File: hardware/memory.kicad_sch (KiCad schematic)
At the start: 5 parts, among them U2 ICE40HX4K-TQ144

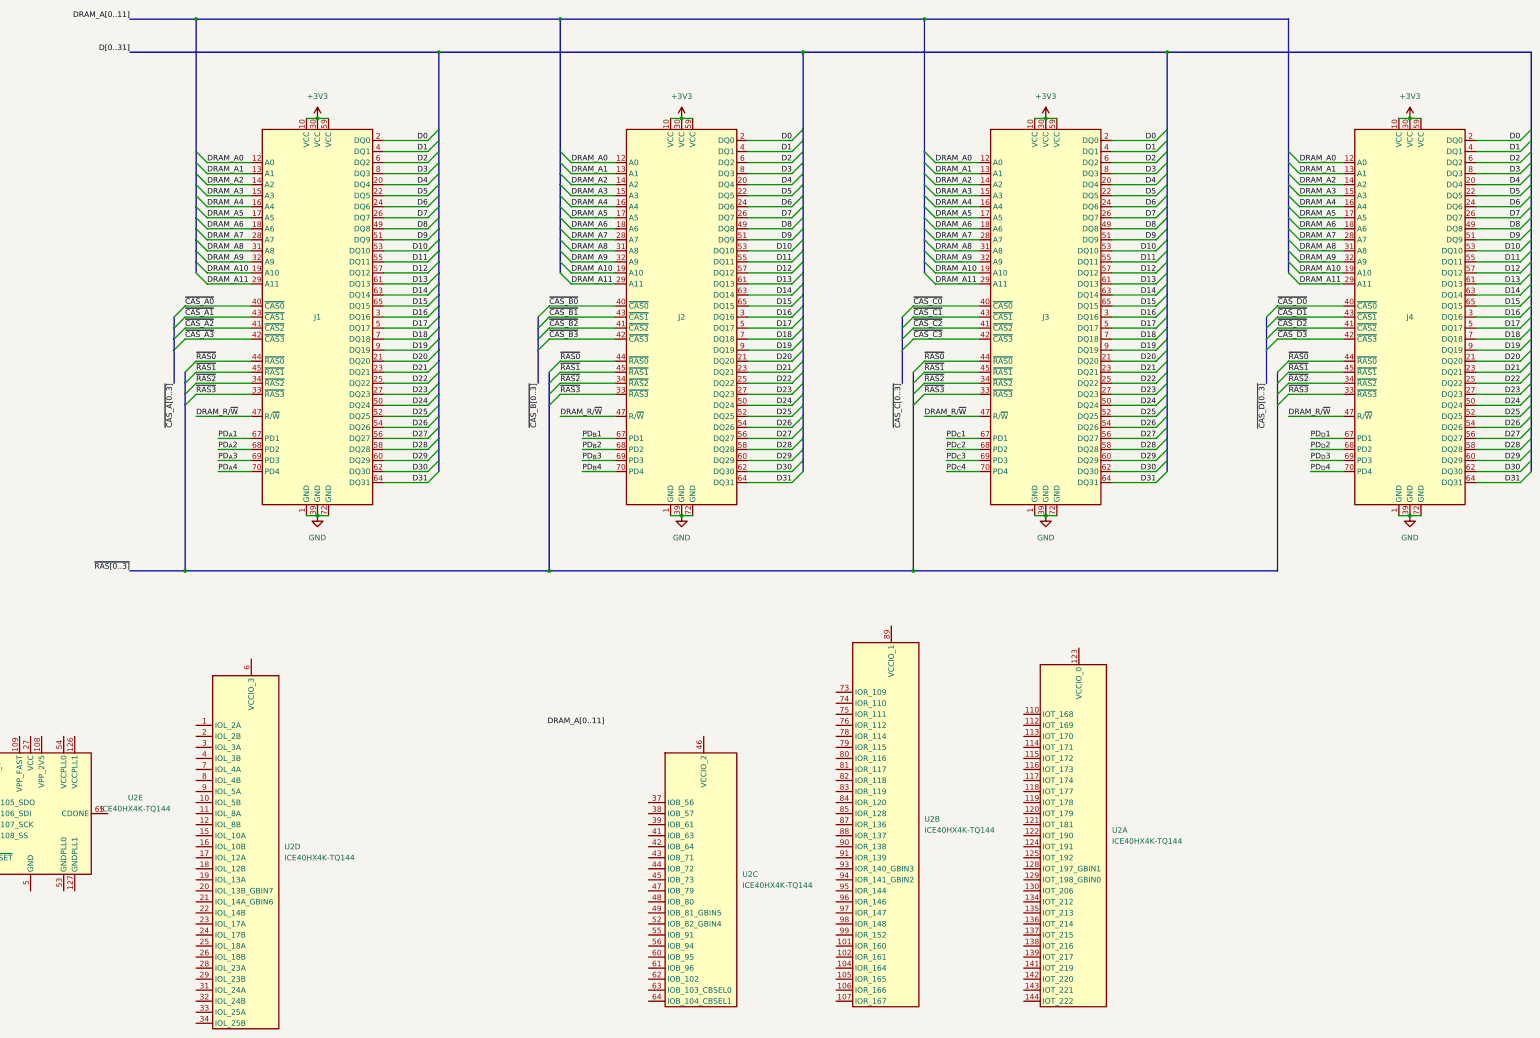
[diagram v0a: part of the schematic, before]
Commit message: more memory wiring
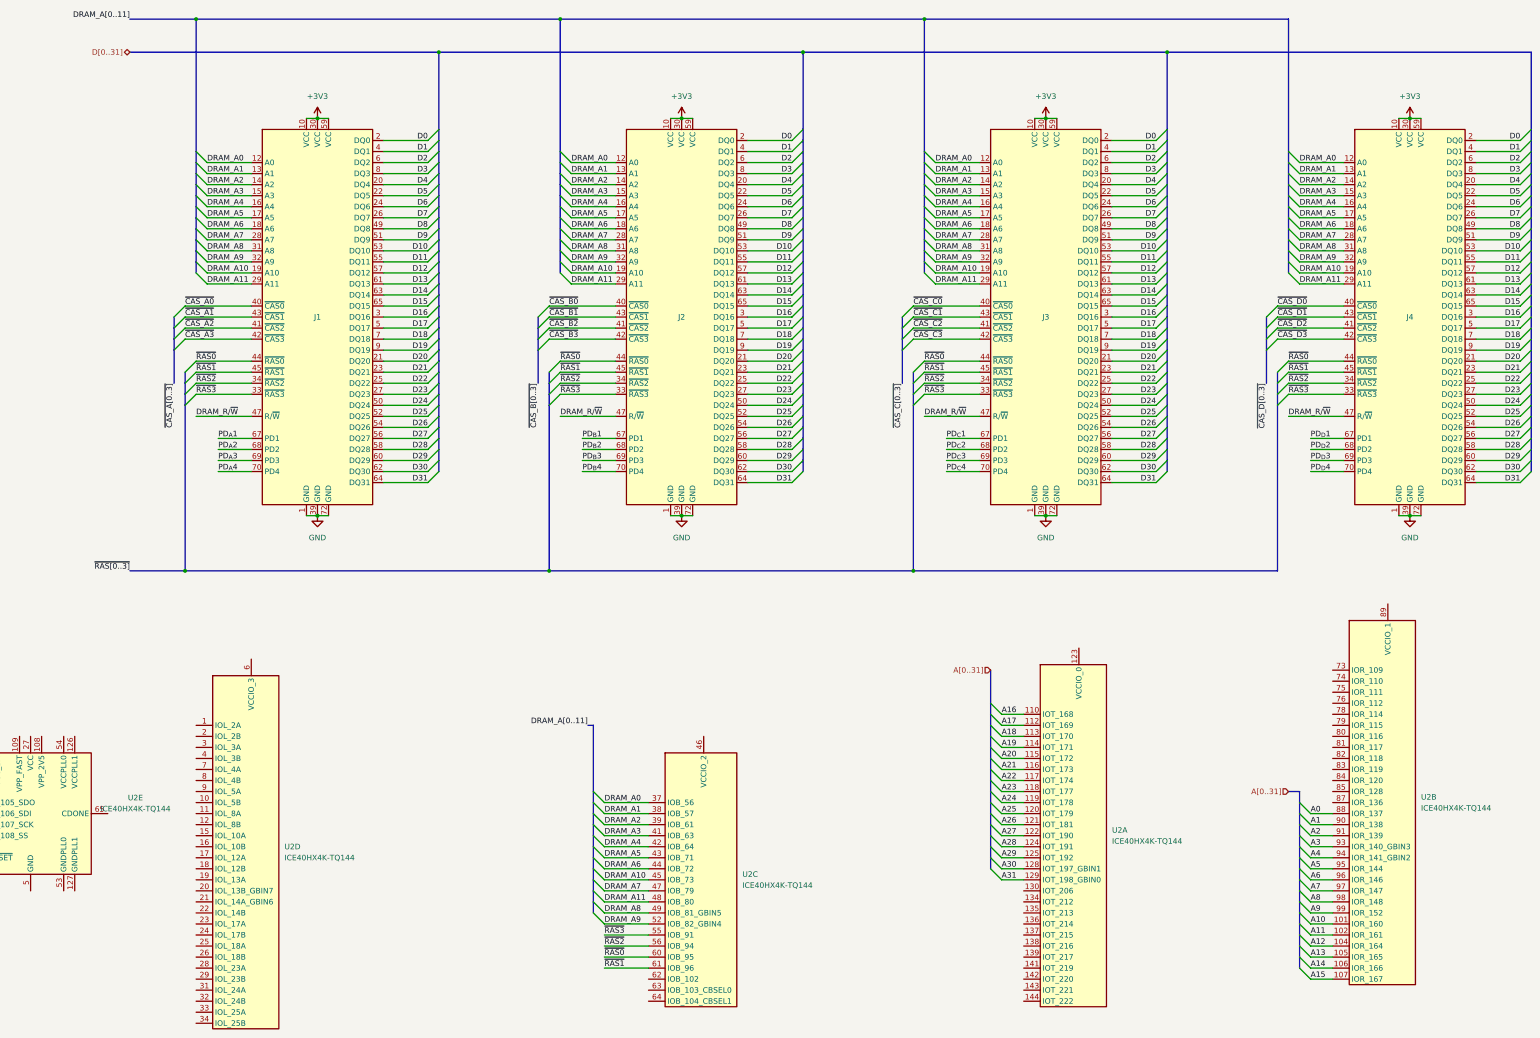
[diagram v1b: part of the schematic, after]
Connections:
- net DRAM_A0: now also U2.37 (IOB_56)
- net DRAM_A1: now also U2.38 (IOB_57)
- net DRAM_A10: now also U2.45 (IOB_73)
- net DRAM_A11: now also U2.48 (IOB_80)
- net DRAM_A2: now also U2.39 (IOB_61)
- net DRAM_A3: now also U2.41 (IOB_63)
- net DRAM_A4: now also U2.42 (IOB_64)
- net DRAM_A5: now also U2.43 (IOB_71)
- net DRAM_A6: now also U2.44 (IOB_72)
- net DRAM_A7: now also U2.47 (IOB_79)
- net DRAM_A8: now also U2.49 (IOB_81_GBIN5)
- net DRAM_A9: now also U2.52 (IOB_82_GBIN4)
- net ~{RAS0}: now also U2.60 (IOB_95)
- net ~{RAS1}: now also U2.61 (IOB_96)
- net ~{RAS2}: now also U2.56 (IOB_94)
- net ~{RAS3}: now also U2.55 (IOB_91)
- net A10: now reaches U2.101 (IOR_160)
- net A11: now reaches U2.102 (IOR_161)
- net A12: now reaches U2.104 (IOR_164)
- net A13: now reaches U2.105 (IOR_165)
- net A14: now reaches U2.106 (IOR_166)
- net A15: now reaches U2.107 (IOR_167)
- net A0: now reaches U2.88 (IOR_137)
- net A1: now reaches U2.90 (IOR_138)
- net A2: now reaches U2.91 (IOR_139)
- net A3: now reaches U2.93 (IOR_140_GBIN3)
- net A4: now reaches U2.94 (IOR_141_GBIN2)
- net A5: now reaches U2.95 (IOR_144)
- net A6: now reaches U2.96 (IOR_146)
- net A7: now reaches U2.97 (IOR_147)
- net A8: now reaches U2.98 (IOR_148)
- net A9: now reaches U2.99 (IOR_152)
- net A16: now reaches U2.110 (IOT_168)
- net A17: now reaches U2.112 (IOT_169)
- net A18: now reaches U2.113 (IOT_170)
- net A19: now reaches U2.114 (IOT_171)
- net A20: now reaches U2.115 (IOT_172)
- net A21: now reaches U2.116 (IOT_173)
- net A22: now reaches U2.117 (IOT_174)
- net A23: now reaches U2.118 (IOT_177)
- net A24: now reaches U2.119 (IOT_178)
- net A25: now reaches U2.120 (IOT_179)
- net A26: now reaches U2.121 (IOT_181)
- net A27: now reaches U2.122 (IOT_190)
- net A28: now reaches U2.124 (IOT_191)
- net A29: now reaches U2.125 (IOT_192)
- net A30: now reaches U2.128 (IOT_197_GBIN1)
- net A31: now reaches U2.129 (IOT_198_GBIN0)
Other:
- moved on the sheet: U2B

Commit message: lock position of expansion slots
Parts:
- J1, J2, J3, J4: footprint 68040:SIMM-72_23DEG -> 68040:SIMM-72
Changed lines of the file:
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@@
       (effects (font (size 1.27 1.27)))
     )
-    (property "Footprint" "68040:SIMM-72_23DEG" (at 287.02 99.06 0)
+    (property "Footprint" "68040:SIMM-72" (at 287.02 99.06 0)
       (effects (font (size 1.27 1.27)) hide)
     )
@@
       (effects (font (size 1.27 1.27)))
     )
-    (property "Footprint" "68040:SIMM-72_23DEG" (at 203.2 99.06 0)
+    (property "Footprint" "68040:SIMM-72" (at 203.2 99.06 0)
       (effects (font (size 1.27 1.27)) hide)
     )
@@
       (effects (font (size 1.27 1.27)))
     )
-    (property "Footprint" "68040:SIMM-72_23DEG" (at 119.38 99.06 0)
+    (property "Footprint" "68040:SIMM-72" (at 119.38 99.06 0)
       (effects (font (size 1.27 1.27)) hide)
     )
@@
       (effects (font (size 1.27 1.27)))
     )
-    (property "Footprint" "68040:SIMM-72_23DEG" (at 370.84 99.06 0)
-      (effects (font (size 1.27 1.27)) hide)
-    )
+    (property "Footprint" "68040:SIMM-72" (at 370.84 99.06 0)
+      (effects (font (size 1.27 1.27)) hide)
+    )

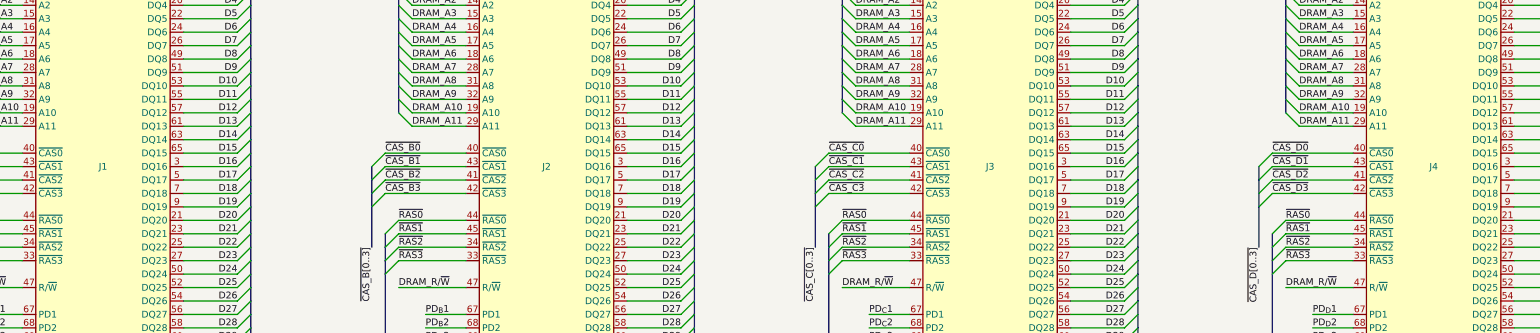
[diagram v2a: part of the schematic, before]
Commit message: fix EXP connector positioning
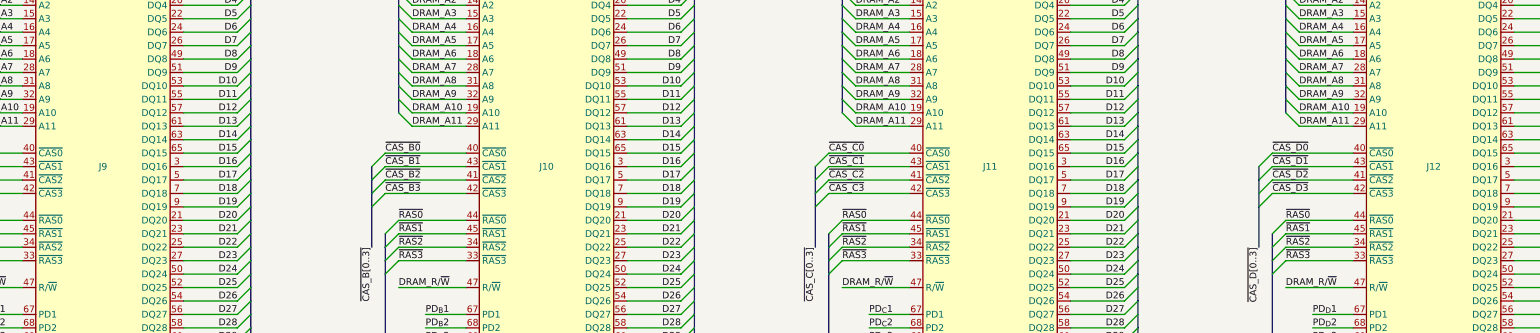
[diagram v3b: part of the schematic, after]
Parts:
- renumbered J2 to J10, J3 to J11, J4 to J12, J1 to J9
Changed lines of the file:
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@@
   (symbol (lib_id "power:+3V3") (at 203.2 55.88 0) (unit 1)
     (in_bom yes) (on_board yes) (dnp no) (fields_autoplaced)
-    (property "Reference" "#PWR07" (at 203.2 59.69 0)
+    (property "Reference" "#PWR03" (at 203.2 59.69 0)
       (effects (font (size 1.27 1.27)) hide)
     )
@@
       (project "68040pc"
         (path "/3006deba-2100-40f8-9f39-987a5c2c14c7/f9007ce6-1d62-4428-abf8-f7bfb8f1e86d"
-          (reference "#PWR07") (unit 1)
+          (reference "#PWR03") (unit 1)
         )
       )
@@
   (symbol (lib_id "power:GND") (at 203.2 147.32 0) (unit 1)
     (in_bom yes) (on_board yes) (dnp no) (fields_autoplaced)
-    (property "Reference" "#PWR02" (at 203.2 153.67 0)
+    (property "Reference" "#PWR04" (at 203.2 153.67 0)
       (effects (font (size 1.27 1.27)) hide)
     )
@@
       (project "68040pc"
         (path "/3006deba-2100-40f8-9f39-987a5c2c14c7/f9007ce6-1d62-4428-abf8-f7bfb8f1e86d"
-          (reference "#PWR02") (unit 1)
+          (reference "#PWR04") (unit 1)
         )
       )
@@
   (symbol (lib_id "68040:SIMM72_Socket") (at 287.02 101.6 0) (unit 1)
     (in_bom yes) (on_board yes) (dnp no) (fields_autoplaced)
-    (property "Reference" "J3" (at 287.02 101.6 0)
+    (property "Reference" "J11" (at 287.02 101.6 0)
       (effects (font (size 1.27 1.27)))
     )
@@
       (project "68040pc"
         (path "/3006deba-2100-40f8-9f39-987a5c2c14c7/f9007ce6-1d62-4428-abf8-f7bfb8f1e86d"
-          (reference "J3") (unit 1)
+          (reference "J11") (unit 1)
         )
       )
@@
   (symbol (lib_id "power:+3V3") (at 370.84 55.88 0) (unit 1)
     (in_bom yes) (on_board yes) (dnp no) (fields_autoplaced)
-    (property "Reference" "#PWR05" (at 370.84 59.69 0)
+    (property "Reference" "#PWR07" (at 370.84 59.69 0)
       (effects (font (size 1.27 1.27)) hide)
     )
@@
       (project "68040pc"
         (path "/3006deba-2100-40f8-9f39-987a5c2c14c7/f9007ce6-1d62-4428-abf8-f7bfb8f1e86d"
-          (reference "#PWR05") (unit 1)
+          (reference "#PWR07") (unit 1)
         )
       )
@@
   (symbol (lib_id "power:GND") (at 370.84 147.32 0) (unit 1)
     (in_bom yes) (on_board yes) (dnp no) (fields_autoplaced)
-    (property "Reference" "#PWR04" (at 370.84 153.67 0)
+    (property "Reference" "#PWR08" (at 370.84 153.67 0)
       (effects (font (size 1.27 1.27)) hide)
     )
@@
       (project "68040pc"
         (path "/3006deba-2100-40f8-9f39-987a5c2c14c7/f9007ce6-1d62-4428-abf8-f7bfb8f1e86d"
-          (reference "#PWR04") (unit 1)
+          (reference "#PWR08") (unit 1)
         )
       )
@@
   (symbol (lib_id "68040:SIMM72_Socket") (at 203.2 101.6 0) (unit 1)
     (in_bom yes) (on_board yes) (dnp no) (fields_autoplaced)
-    (property "Reference" "J2" (at 203.2 101.6 0)
+    (property "Reference" "J10" (at 203.2 101.6 0)
       (effects (font (size 1.27 1.27)))
     )
@@
       (project "68040pc"
         (path "/3006deba-2100-40f8-9f39-987a5c2c14c7/f9007ce6-1d62-4428-abf8-f7bfb8f1e86d"
-          (reference "J2") (unit 1)
+          (reference "J10") (unit 1)
         )
       )
@@
   (symbol (lib_id "68040:SIMM72_Socket") (at 119.38 101.6 0) (unit 1)
     (in_bom yes) (on_board yes) (dnp no) (fields_autoplaced)
-    (property "Reference" "J1" (at 119.38 101.6 0)
+    (property "Reference" "J9" (at 119.38 101.6 0)
       (effects (font (size 1.27 1.27)))
     )
@@
       (project "68040pc"
         (path "/3006deba-2100-40f8-9f39-987a5c2c14c7/f9007ce6-1d62-4428-abf8-f7bfb8f1e86d"
-          (reference "J1") (unit 1)
+          (reference "J9") (unit 1)
         )
       )
@@
   (symbol (lib_id "power:+3V3") (at 287.02 55.88 0) (unit 1)
     (in_bom yes) (on_board yes) (dnp no) (fields_autoplaced)
-    (property "Reference" "#PWR06" (at 287.02 59.69 0)
+    (property "Reference" "#PWR05" (at 287.02 59.69 0)
       (effects (font (size 1.27 1.27)) hide)
     )
@@
       (project "68040pc"
         (path "/3006deba-2100-40f8-9f39-987a5c2c14c7/f9007ce6-1d62-4428-abf8-f7bfb8f1e86d"
-          (reference "#PWR06") (unit 1)
+          (reference "#PWR05") (unit 1)
         )
       )
@@
   (symbol (lib_id "power:GND") (at 119.38 147.32 0) (unit 1)
     (in_bom yes) (on_board yes) (dnp no) (fields_autoplaced)
-    (property "Reference" "#PWR03" (at 119.38 153.67 0)
+    (property "Reference" "#PWR02" (at 119.38 153.67 0)
       (effects (font (size 1.27 1.27)) hide)
     )
@@
       (project "68040pc"
         (path "/3006deba-2100-40f8-9f39-987a5c2c14c7/f9007ce6-1d62-4428-abf8-f7bfb8f1e86d"
-          (reference "#PWR03") (unit 1)
+          (reference "#PWR02") (unit 1)
         )
       )
@@
   (symbol (lib_id "power:GND") (at 287.02 147.32 0) (unit 1)
     (in_bom yes) (on_board yes) (dnp no) (fields_autoplaced)
-    (property "Reference" "#PWR01" (at 287.02 153.67 0)
+    (property "Reference" "#PWR06" (at 287.02 153.67 0)
       (effects (font (size 1.27 1.27)) hide)
     )
@@
       (project "68040pc"
         (path "/3006deba-2100-40f8-9f39-987a5c2c14c7/f9007ce6-1d62-4428-abf8-f7bfb8f1e86d"
+          (reference "#PWR06") (unit 1)
+        )
+      )
+    )
+  )
+  (symbol (lib_id "power:+3V3") (at 119.38 55.88 0) (unit 1)
+    (in_bom yes) (on_board yes) (dnp no) (fields_autoplaced)
+    (property "Reference" "#PWR01" (at 119.38 59.69 0)
+      (effects (font (size 1.27 1.27)) hide)
+    )
+    (property "Value" "+3V3" (at 119.38 50.8 0)
+      (effects (font (size 1.27 1.27)))
+    )
+    (property "Footprint" "" (at 119.38 55.88 0)
+      (effects (font (size 1.27 1.27)) hide)
+    )
+    (property "Datasheet" "" (at 119.38 55.88 0)
+      (effects (font (size 1.27 1.27)) hide)
+    )
+    (pin "1")
+    (instances
+      (project "68040pc"
+        (path "/3006deba-2100-40f8-9f39-987a5c2c14c7/f9007ce6-1d62-4428-abf8-f7bfb8f1e86d"
           (reference "#PWR01") (unit 1)
         )
@@
     )
   )
-  (symbol (lib_id "power:+3V3") (at 119.38 55.88 0) (unit 1)
-    (in_bom yes) (on_board yes) (dnp no) (fields_autoplaced)
-    (property "Reference" "#PWR08" (at 119.38 59.69 0)
-      (effects (font (size 1.27 1.27)) hide)
-    )
-    (property "Value" "+3V3" (at 119.38 50.8 0)
-      (effects (font (size 1.27 1.27)))
-    )
-    (property "Footprint" "" (at 119.38 55.88 0)
-      (effects (font (size 1.27 1.27)) hide)
-    )
-    (property "Datasheet" "" (at 119.38 55.88 0)
-      (effects (font (size 1.27 1.27)) hide)
-    )
-    (pin "1")
-    (instances
-      (project "68040pc"
-        (path "/3006deba-2100-40f8-9f39-987a5c2c14c7/f9007ce6-1d62-4428-abf8-f7bfb8f1e86d"
-          (reference "#PWR08") (unit 1)
-        )
-      )
-    )
-  )
   (symbol (lib_id "68040:SIMM72_Socket") (at 370.84 101.6 0) (unit 1)
     (in_bom yes) (on_board yes) (dnp no) (fields_autoplaced)
-    (property "Reference" "J4" (at 370.84 101.6 0)
+    (property "Reference" "J12" (at 370.84 101.6 0)
       (effects (font (size 1.27 1.27)))
     )
@@
       (project "68040pc"
         (path "/3006deba-2100-40f8-9f39-987a5c2c14c7/f9007ce6-1d62-4428-abf8-f7bfb8f1e86d"
-          (reference "J4") (unit 1)
-        )
-      )
+          (reference "J12") (unit 1)
+        )
+      )
